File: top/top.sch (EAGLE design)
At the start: 10 parts, among them X1 52745-1290

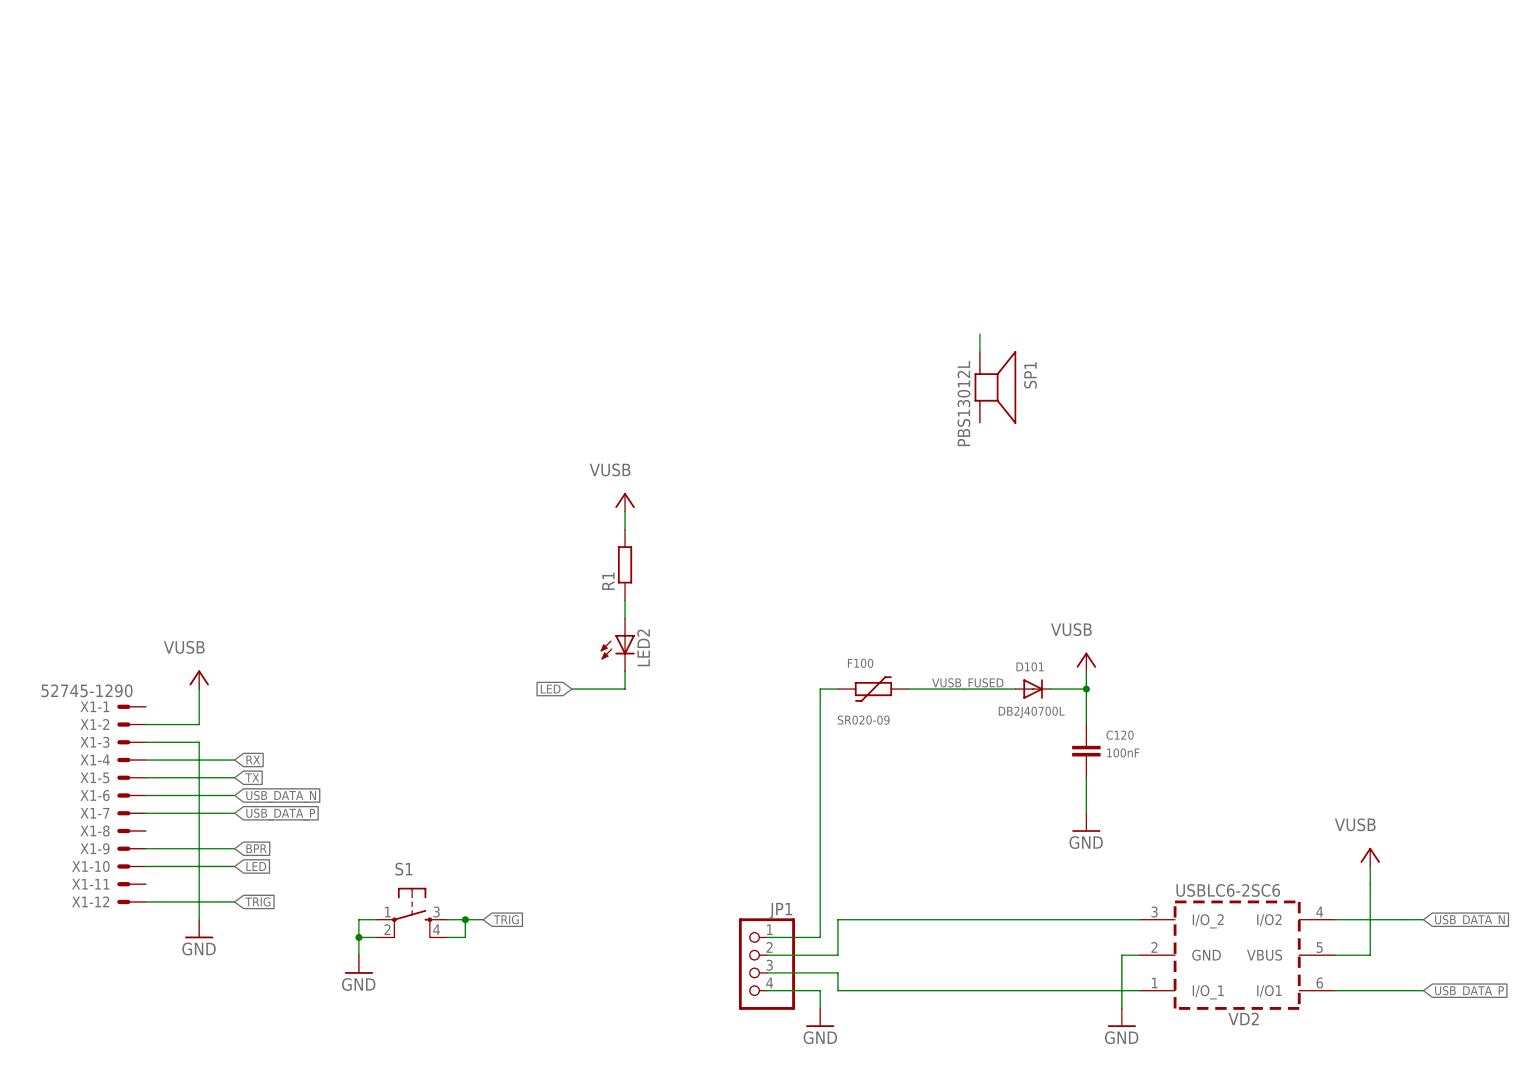
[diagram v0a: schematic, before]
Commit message: Added silkscreen texts
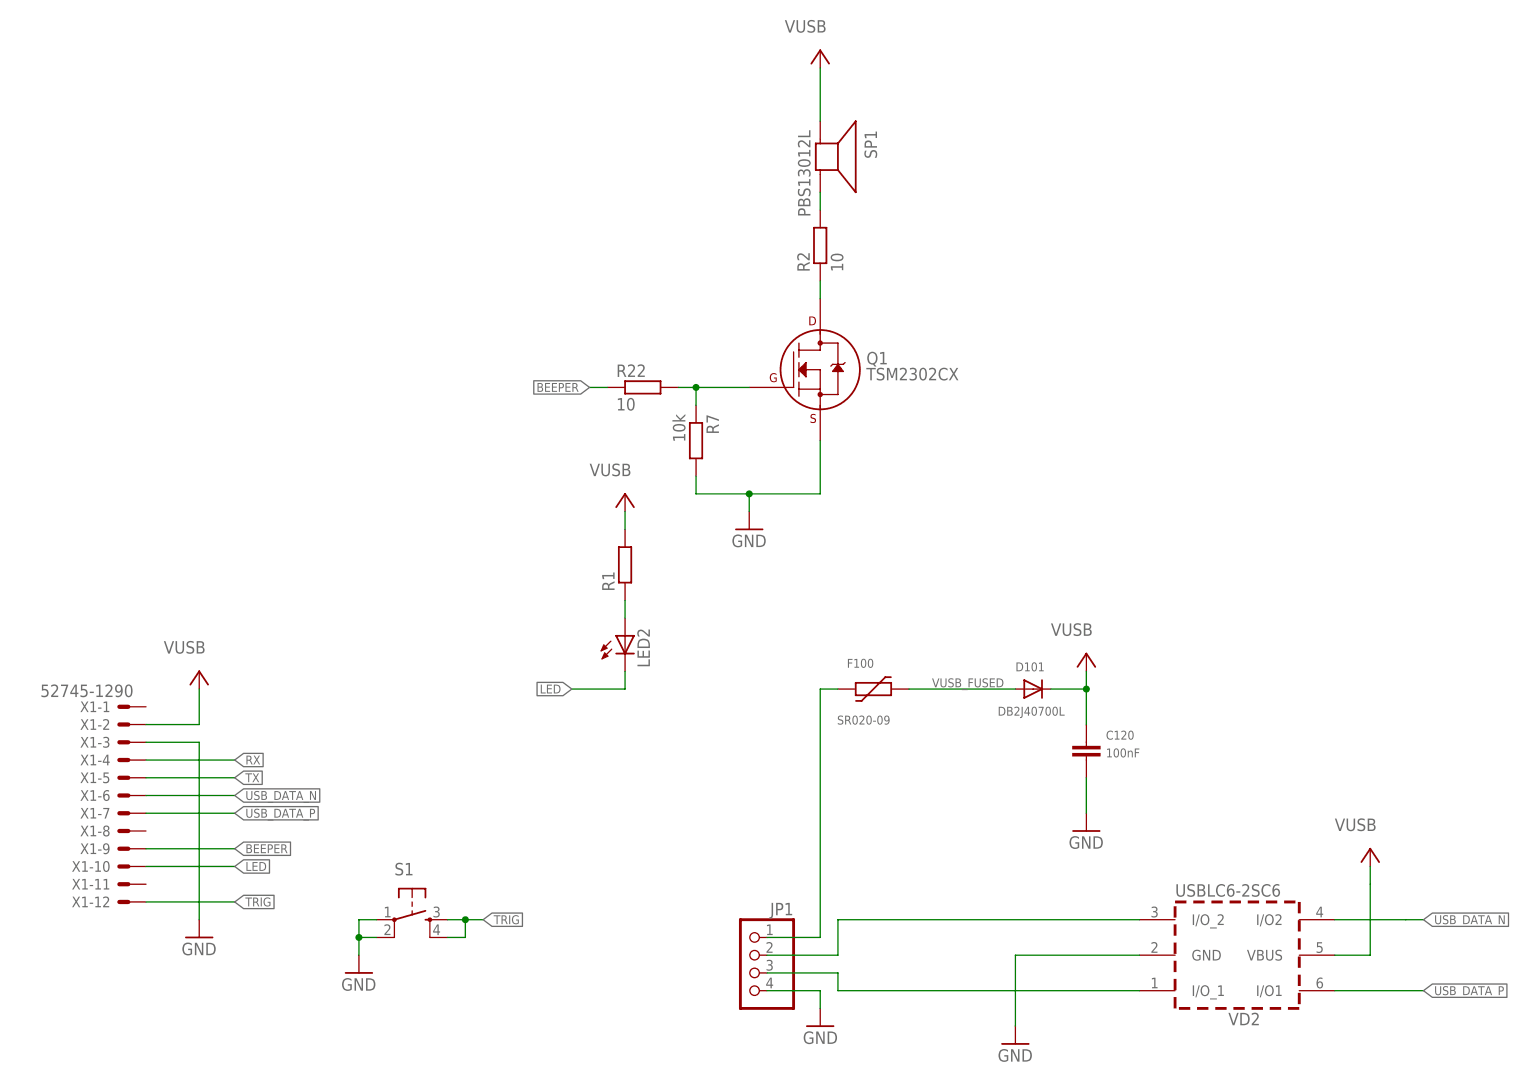
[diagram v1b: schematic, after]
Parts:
- added Q1: TSM2302CX, transistors:2N7002A_SOT23
- added R2, R22: 10, rcl:R-EU_R0603
- added R7: 10k, rcl:R-EU_R0603
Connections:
- net N$1 renamed LED_R
- removed net BPR: X1-9.S
- removed net BUZZER_PLUS: SP1.+
- new net BEEPER: R22.1, X1-9.S
- new net BEEPER_FET_DRAIN: Q1.D, R2.1
- new net BEEPER_R: R2.2, SP1.-
- new net BUZZER_BEFORERES: Q1.G, R22.2, R7.1
- net GND: now also Q1.S, R7.2
- net VUSB: now also SP1.+
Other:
- moved on the sheet: SP1
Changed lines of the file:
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@@
 <?xml version="1.0" encoding="utf-8"?>
 <!DOCTYPE eagle SYSTEM "eagle.dtd">
-<eagle version="9.4.2">
+<eagle version="9.6.2">
 <drawing>
 <settings>
@@
 <attribute name="OC_LOMEX" value="46-02-60"/>
 </part>
-<part name="JP1" library="pinhead" library_urn="urn:adsk.eagle:library:325" deviceset="PINHD-1X4" device="" package3d_urn="urn:adsk.eagle:package:22407/2"/>
+<part name="JP1" library="pinhead" deviceset="PINHD-1X4" device=""/>
 <part name="GND4" library="supply1" deviceset="GND" device=""/>
 <part name="VD2" library="usblc6" deviceset="USBLC6-2" device="SC6" value="USBLC6-2SC6">
@@
 <part name="P+4" library="supply1" deviceset="VUSB" device=""/>
 <part name="GND2" library="supply1" deviceset="GND" device=""/>
+<part name="R7" library="rcl" deviceset="R-EU_" device="R0603" value="10k"/>
+<part name="Q1" library="transistors" deviceset="2N700*" device="_SOT23" technology="2A" value="TSM2302CX"/>
+<part name="GND33" library="SparkFun" deviceset="GND" device=""/>
+<part name="R22" library="rcl" deviceset="R-EU_" device="R0603" value="10"/>
+<part name="R2" library="rcl" deviceset="R-EU_" device="R0603" value="10"/>
+<part name="P+2" library="supply1" deviceset="VUSB" device=""/>
 </parts>
 <sheets>
@@
 <attribute name="VALUE" x="127.635" y="48.768" size="1.778" layer="96" rot="R90"/>
 </instance>
-<instance part="SP1" gate="S1" x="172.72" y="88.9" smashed="yes" rot="R270">
-<attribute name="OC_LOMEX" x="172.72" y="88.9" size="1.778" layer="96" rot="R270" display="off"/>
-<attribute name="NAME" x="179.07" y="92.71" size="1.778" layer="95" rot="R270"/>
-<attribute name="VALUE" x="169.545" y="92.71" size="1.778" layer="96" rot="R270"/>
+<instance part="SP1" gate="S1" x="149.86" y="121.92" smashed="yes" rot="R270">
+<attribute name="OC_LOMEX" x="149.86" y="121.92" size="1.778" layer="96" rot="R270" display="off"/>
+<attribute name="NAME" x="156.21" y="125.73" size="1.778" layer="95" rot="R270"/>
+<attribute name="VALUE" x="146.685" y="125.73" size="1.778" layer="96" rot="R270"/>
 </instance>
 <instance part="JP1" gate="A" x="139.7" y="5.08" smashed="yes" rot="MR0">
@@
 <attribute name="OC_HQ" x="210.82" y="7.62" size="1.27" layer="96" rot="MR180" display="off"/>
 </instance>
-<instance part="GND5" gate="1" x="193.04" y="-2.54" smashed="yes">
-<attribute name="VALUE" x="190.5" y="-5.08" size="1.778" layer="96"/>
+<instance part="GND5" gate="1" x="177.8" y="-5.08" smashed="yes">
+<attribute name="VALUE" x="175.26" y="-7.62" size="1.778" layer="96"/>
 </instance>
 <instance part="P+6" gate="G$1" x="228.6" y="22.86" smashed="yes">
@@
 <instance part="GND2" gate="1" x="187.96" y="25.4" smashed="yes">
 <attribute name="VALUE" x="185.42" y="22.86" size="1.778" layer="96"/>
+</instance>
+<instance part="R7" gate="G$1" x="132.08" y="81.28" smashed="yes" rot="R270">
+<attribute name="NAME" x="133.5786" y="85.09" size="1.778" layer="95" rot="R270"/>
+<attribute name="VALUE" x="128.778" y="85.09" size="1.778" layer="96" rot="R270"/>
+</instance>
+<instance part="Q1" gate="G$1" x="149.86" y="91.44" smashed="yes">
+<attribute name="NAME" x="156.464" y="92.202" size="1.778" layer="95"/>
+<attribute name="VALUE" x="156.464" y="89.916" size="1.778" layer="96"/>
+</instance>
+<instance part="GND33" gate="1" x="139.7" y="68.58" smashed="yes">
+<attribute name="VALUE" x="137.16" y="66.04" size="1.778" layer="96"/>
+</instance>
+<instance part="R22" gate="G$1" x="124.46" y="88.9" smashed="yes">
+<attribute name="NAME" x="120.65" y="90.3986" size="1.778" layer="95"/>
+<attribute name="VALUE" x="120.65" y="85.598" size="1.778" layer="96"/>
+</instance>
+<instance part="R2" gate="G$1" x="149.86" y="109.22" smashed="yes" rot="R90">
+<attribute name="NAME" x="148.3614" y="105.41" size="1.778" layer="95" rot="R90"/>
+<attribute name="VALUE" x="153.162" y="105.41" size="1.778" layer="96" rot="R90"/>
+</instance>
+<instance part="P+2" gate="G$1" x="149.86" y="137.16" smashed="yes">
+<attribute name="VALUE" x="144.78" y="139.7" size="1.778" layer="96"/>
 </instance>
 </instances>
@@
 <pinref part="P+4" gate="G$1" pin="VUSB"/>
 <wire x1="187.96" y1="48.26" x2="187.96" y2="45.72" width="0.1524" layer="91"/>
+</segment>
+<segment>
+<pinref part="SP1" gate="S1" pin="+"/>
+<wire x1="149.86" y1="127" x2="149.86" y2="134.62" width="0.1524" layer="91"/>
+<pinref part="P+2" gate="G$1" pin="VUSB"/>
 </segment>
 </net>
@@
 <segment>
 <pinref part="VD2" gate="G$1" pin="GND"/>
-<wire x1="195.58" y1="7.62" x2="193.04" y2="7.62" width="0.1524" layer="91"/>
+<wire x1="195.58" y1="7.62" x2="177.8" y2="7.62" width="0.1524" layer="91"/>
 <pinref part="GND5" gate="1" pin="GND"/>
-<wire x1="193.04" y1="7.62" x2="193.04" y2="0" width="0.1524" layer="91"/>
+<wire x1="177.8" y1="7.62" x2="177.8" y2="-2.54" width="0.1524" layer="91"/>
 </segment>
 <segment>
@@
 <wire x1="187.96" y1="27.94" x2="187.96" y2="33.02" width="0.1524" layer="91"/>
 <pinref part="GND2" gate="1" pin="GND"/>
+</segment>
+<segment>
+<pinref part="R7" gate="G$1" pin="2"/>
+<wire x1="132.08" y1="76.2" x2="132.08" y2="73.66" width="0.1524" layer="91"/>
+<pinref part="Q1" gate="G$1" pin="S"/>
+<wire x1="132.08" y1="73.66" x2="139.7" y2="73.66" width="0.1524" layer="91"/>
+<wire x1="139.7" y1="73.66" x2="149.86" y2="73.66" width="0.1524" layer="91"/>
+<wire x1="149.86" y1="73.66" x2="149.86" y2="81.28" width="0.1524" layer="91"/>
+<pinref part="GND33" gate="1" pin="GND"/>
+<wire x1="139.7" y1="71.12" x2="139.7" y2="73.66" width="0.1524" layer="91"/>
+<junction x="139.7" y="73.66"/>
 </segment>
 </net>
@@
 </segment>
 </net>
-<net name="BPR" class="0">
+<net name="BEEPER" class="0">
 <segment>
 <pinref part="X1" gate="-9" pin="S"/>
 <wire x1="53.34" y1="22.86" x2="66.04" y2="22.86" width="0.1524" layer="91"/>
 <label x="66.04" y="22.86" size="1.27" layer="95" font="vector" xref="yes"/>
+</segment>
+<segment>
+<pinref part="R22" gate="G$1" pin="1"/>
+<wire x1="119.38" y1="88.9" x2="116.84" y2="88.9" width="0.1524" layer="91"/>
+<label x="116.84" y="88.9" size="1.27" layer="95" rot="R180" xref="yes"/>
 </segment>
 </net>
@@
 </segment>
 </net>
-<net name="N$1" class="0">
+<net name="LED_R" class="0">
 <segment>
 <pinref part="R1" gate="G$1" pin="1"/>
 <wire x1="121.92" y1="58.42" x2="121.92" y2="55.88" width="0.1524" layer="91"/>
 <pinref part="LED2" gate="G$1" pin="A"/>
-</segment>
-</net>
-<net name="BUZZER_PLUS" class="0">
-<segment>
-<pinref part="SP1" gate="S1" pin="+"/>
-<wire x1="172.72" y1="93.98" x2="172.72" y2="96.52" width="0.1524" layer="91"/>
 </segment>
 </net>
@@
 </segment>
 </net>
+<net name="BUZZER_BEFORERES" class="0">
+<segment>
+<pinref part="Q1" gate="G$1" pin="G"/>
+<pinref part="R7" gate="G$1" pin="1"/>
+<wire x1="139.7" y1="88.9" x2="132.08" y2="88.9" width="0.1524" layer="91"/>
+<wire x1="132.08" y1="88.9" x2="132.08" y2="86.36" width="0.1524" layer="91"/>
+<pinref part="R22" gate="G$1" pin="2"/>
+<wire x1="132.08" y1="88.9" x2="129.54" y2="88.9" width="0.1524" layer="91"/>
+<junction x="132.08" y="88.9"/>
+</segment>
+</net>
+<net name="BEEPER_FET_DRAIN" class="0">
+<segment>
+<pinref part="Q1" gate="G$1" pin="D"/>
+<pinref part="R2" gate="G$1" pin="1"/>
+<wire x1="149.86" y1="104.14" x2="149.86" y2="101.6" width="0.1524" layer="91"/>
+</segment>
+</net>
+<net name="BEEPER_R" class="0">
+<segment>
+<pinref part="R2" gate="G$1" pin="2"/>
+<pinref part="SP1" gate="S1" pin="-"/>
+<wire x1="149.86" y1="116.84" x2="149.86" y2="114.3" width="0.1524" layer="91"/>
+</segment>
+</net>
 </nets>
 </sheet>
@@
 </schematic>
 </drawing>
-<compatibility>
-<note version="8.2" severity="warning">
-Since Version 8.2, EAGLE supports online libraries. The ids
-of those online libraries will not be understood (or retained)
-with this version.
-</note>
-<note version="8.3" severity="warning">
-Since Version 8.3, EAGLE supports URNs for individual library
-assets (packages, symbols, and devices). The URNs of those assets
-will not be understood (or retained) with this version.
-</note>
-<note version="8.3" severity="warning">
-Since Version 8.3, EAGLE supports the association of 3D packages
-with devices in libraries, schematics, and board files. Those 3D
-packages will not be understood (or retained) with this version.
-</note>
-</compatibility>
 </eagle>
